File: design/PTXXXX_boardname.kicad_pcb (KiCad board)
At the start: 2 copper layers, 1 part

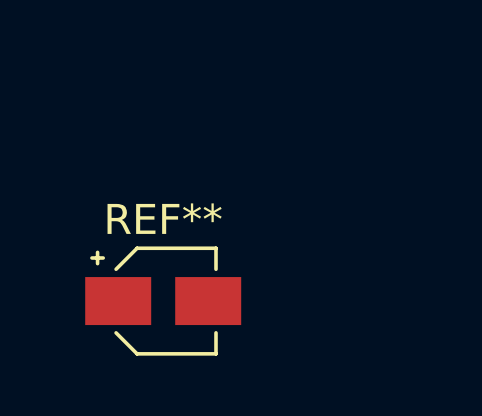
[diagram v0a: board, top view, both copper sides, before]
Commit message: updated PCB from netlist
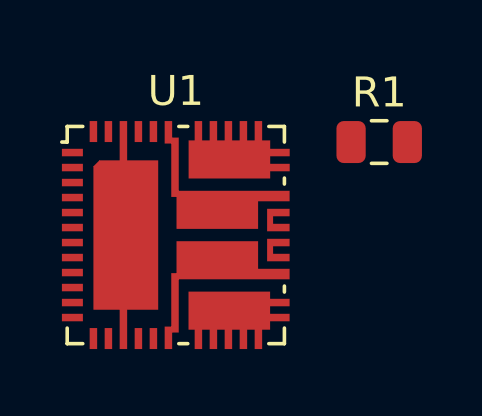
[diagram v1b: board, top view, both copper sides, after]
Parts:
- removed REF**: CP_Elec_3x5.3, Capacitor_SMD:CP_Elec_3x5.3
- added R1: 1k, Resistor_SMD:R_0805_2012Metric, F.Cu at (127.3, 74.2)
- added U1: IR4302, Package_DFN_QFN:Infineon_PQFN-44-31-5EP_7x7mm_P0.5mm, F.Cu at (120.5, 77.3)
